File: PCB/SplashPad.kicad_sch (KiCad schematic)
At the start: 34 parts, among them SW1 SW_Push_45deg, SW10 RotaryEncoder_Switch, SW2 SW_Push_45deg, SW3 SW_Push_45deg, SW4 SW_Push_45deg, SW5 SW_Push_45deg, SW6 SW_Push_45deg, SW7 SW_Push_45deg, SW8 SW_Push_45deg, SW9 SW_Push_45deg, U1 XIAO-RP2040-DIP

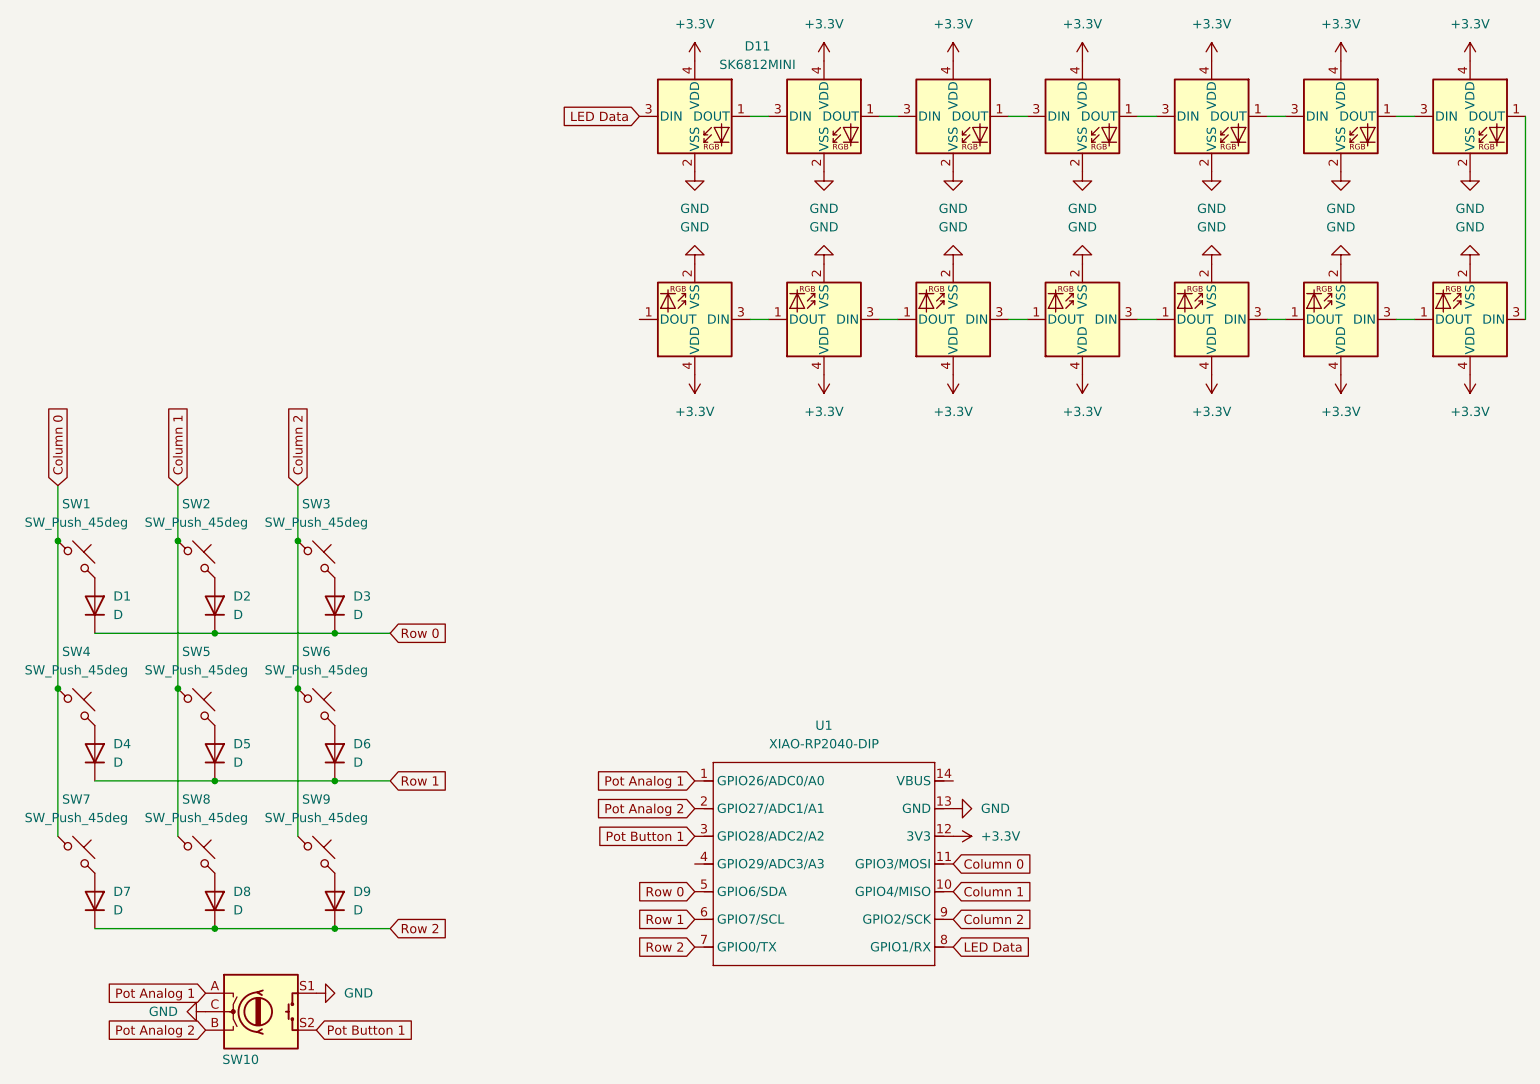
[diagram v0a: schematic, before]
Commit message: LED Voltage Fix
I thought they worked at 3.3v oopsies
I also had the encoder wired wrong and fixed that.
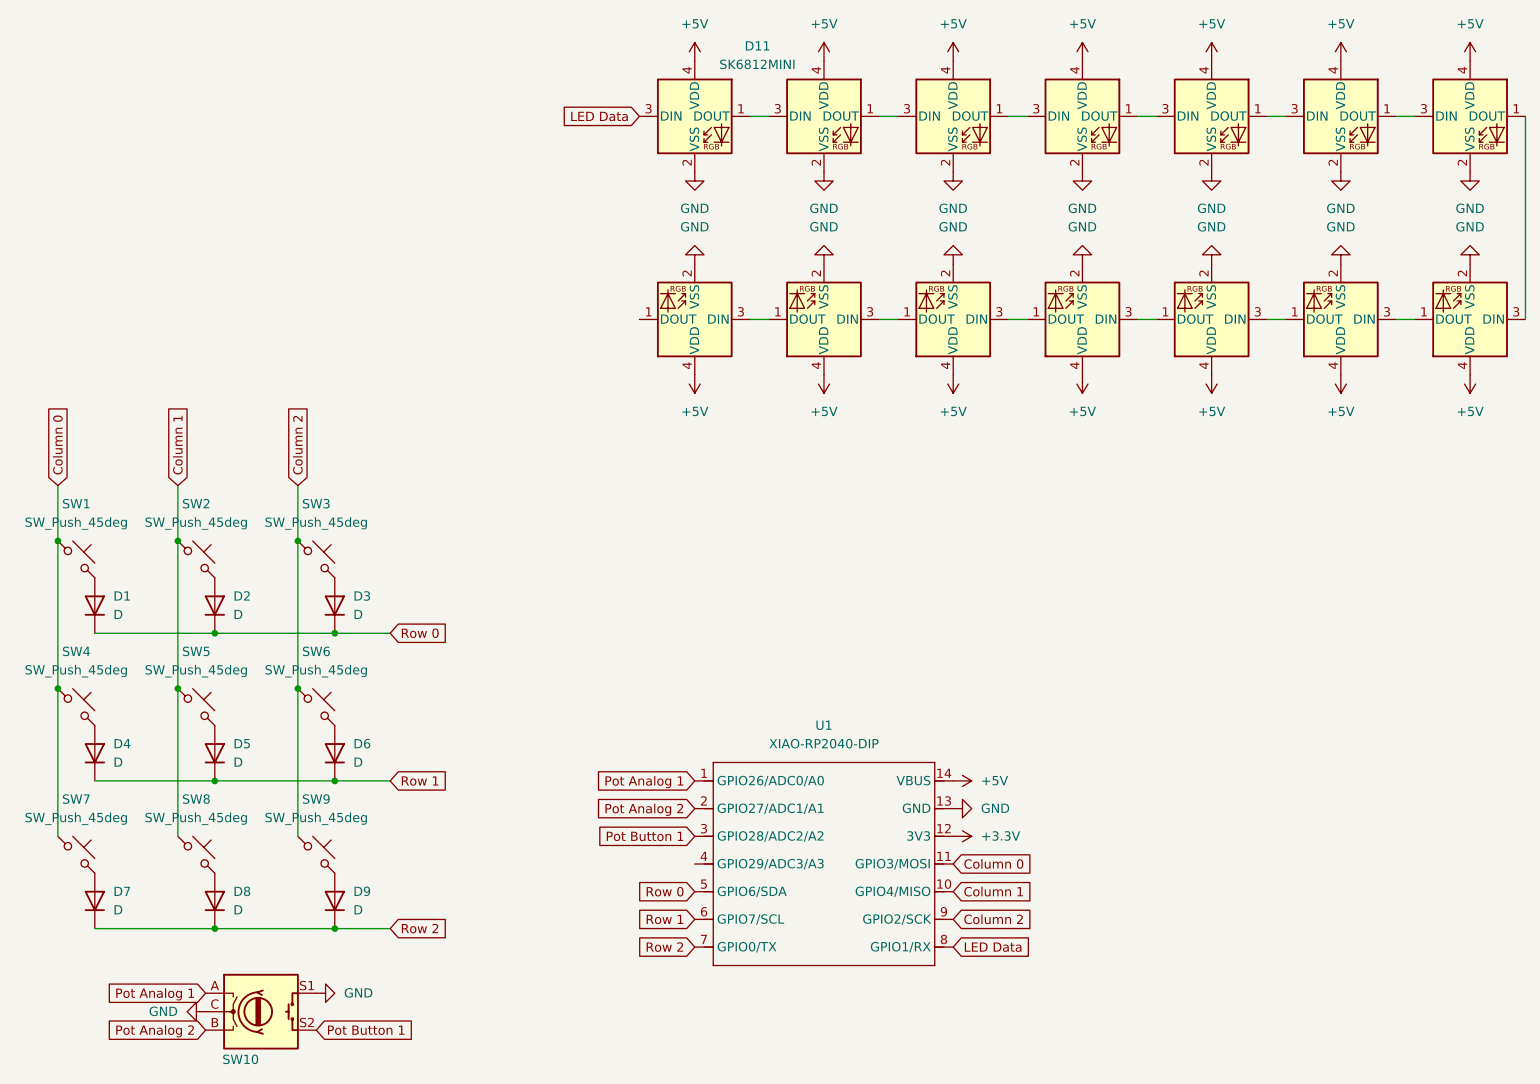
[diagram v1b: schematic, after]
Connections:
- net +3.3V: no longer D10.4 (VDD), D11.4 (VDD), D12.4 (VDD), D13.4 (VDD), D14.4 (VDD), D15.4 (VDD), D16.4 (VDD), D17.4 (VDD), D18.4 (VDD), D19.4 (VDD), D20.4 (VDD), D21.4 (VDD), D22.4 (VDD), D23.4 (VDD)
- net +5V: now reaches U1.14 (VBUS)
- net +5V: now also D10.4 (VDD), D11.4 (VDD), D12.4 (VDD), D13.4 (VDD), D14.4 (VDD), D15.4 (VDD), D16.4 (VDD), D17.4 (VDD), D18.4 (VDD), D19.4 (VDD), D20.4 (VDD), D21.4 (VDD), D22.4 (VDD), D23.4 (VDD)
